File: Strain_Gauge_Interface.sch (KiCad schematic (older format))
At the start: 5 parts, among them U2 INA828

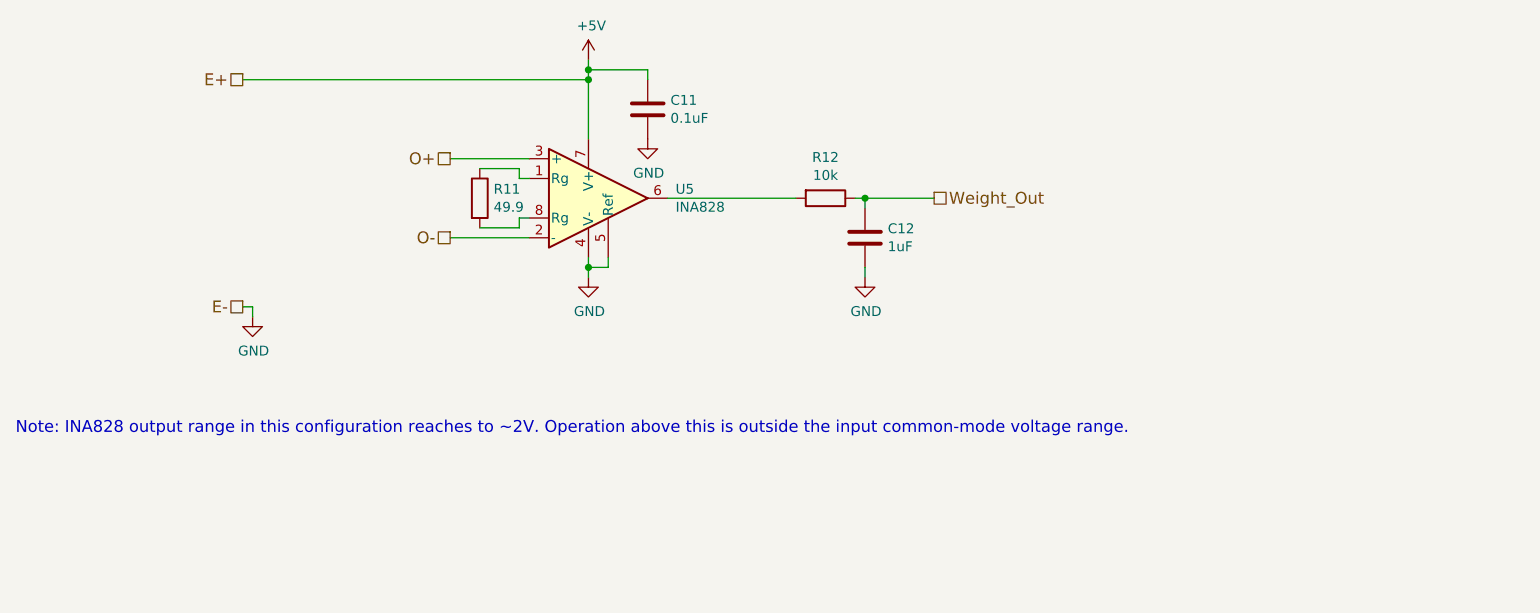
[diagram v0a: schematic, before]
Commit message: Pretty much ready to go. Should verify barrel jack first. Needs a logo.
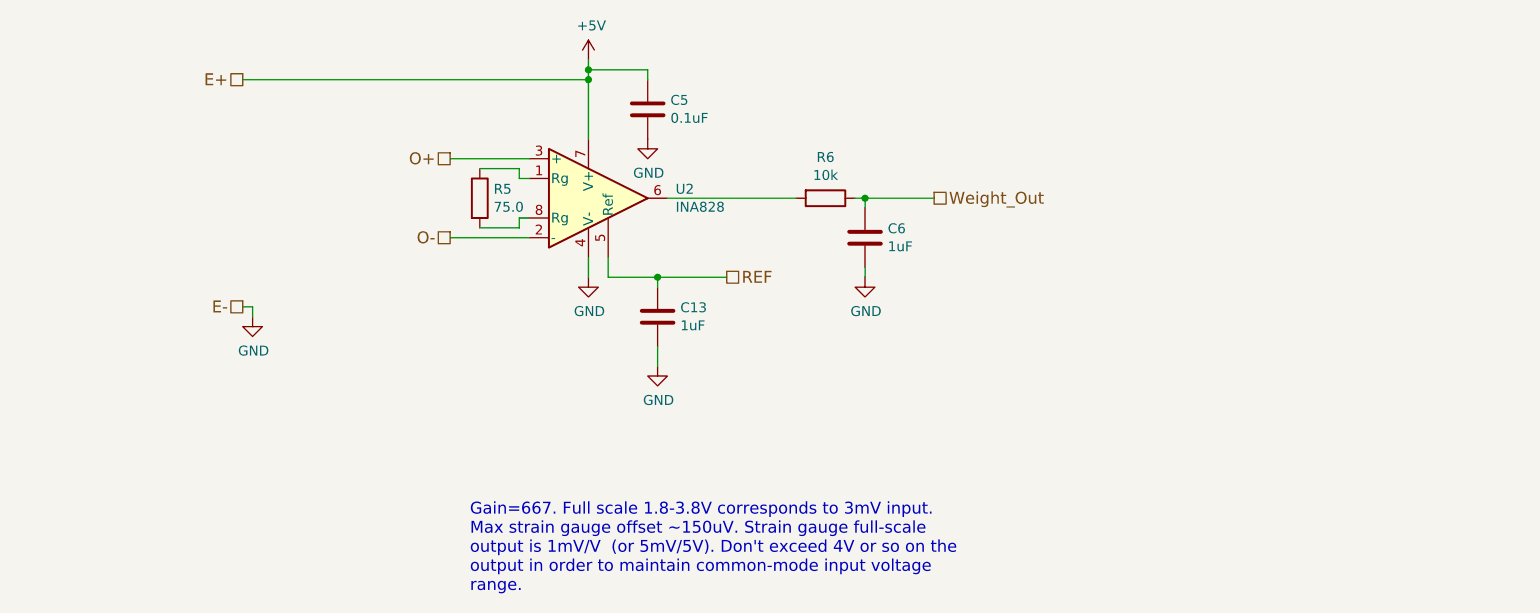
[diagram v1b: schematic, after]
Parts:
- added C16: 1uF, Capacitors_SMD:C_0805_HandSoldering, symbol device:C
- R5: value 49.9 -> 75.0
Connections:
- net GND: now also C16.2; no longer U2.5 (Ref)
- new net REF: C16.1, U2.5 (Ref)
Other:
- note added: "Gain=667. Full scale 1.8-3.8V corresponds to 3mV input.\nMax strain gauge offset ~~150uV. Strain gauge full-scale \noutput is 1mV/V (or 5mV/5V). Don't exceed 4V or so on the\noutput in order to maintain common-mode input voltage\nrange."
- note removed: "Note: INA828 output range in this configuration reaches to ~~2V. Operation above this is outside the input common-mode voltage range."
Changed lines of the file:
@@
 $Descr A4 11693 8268
 encoding utf-8
-Sheet 3 8
+Sheet 7 9
 Title ""
 Date ""
@@
 AR Path="/5A46629B/5A4C63BA" Ref="U3"  Part="1"
 AR Path="/5A4663D1/5A4C63BA" Ref="U4"  Part="1"
-F 0 "U5" H 5041 3546 50  0000 L CNN
+F 0 "U2" H 5041 3546 50  0000 L CNN
 F 1 "INA828" H 5041 3455 50  0000 L CNN
 F 2 "Housings_SOIC:SOIC-8_3.9x4.9mm_Pitch1.27mm" H 4700 3500 50  0001 C CNN
@@
 AR Path="/5A46629B/5A4C64A7" Ref="R7"  Part="1"
 AR Path="/5A4663D1/5A4C64A7" Ref="R9"  Part="1"
-F 0 "R11" H 4120 3546 50  0000 L CNN
-F 1 "49.9" H 4120 3455 50  0000 L CNN
+F 0 "R5" H 4120 3546 50  0000 L CNN
+F 1 "75.0" H 4120 3455 50  0000 L CNN
 F 2 "Resistors_SMD:R_0805_HandSoldering" V 3980 3500 50  0001 C CNN
 F 3 "" H 4050 3500 50  0001 C CNN
@@
 AR Path="/5A46629B/5A4C656F" Ref="C7"  Part="1"
 AR Path="/5A4663D1/5A4C656F" Ref="C9"  Part="1"
-F 0 "C11" H 5015 3096 50  0000 L CNN
+F 0 "C5" H 5015 3096 50  0000 L CNN
 F 1 "0.1uF" H 5015 3005 50  0000 L CNN
 F 2 "Capacitors_SMD:C_0805_HandSoldering" H 4938 2900 50  0001 C CNN
@@
 AR Path="/5A46629B/5A4C6EE8" Ref="R8"  Part="1"
 AR Path="/5A4663D1/5A4C6EE8" Ref="R10"  Part="1"
-F 0 "R12" V 5593 3500 50  0000 C CNN
+F 0 "R6" V 5593 3500 50  0000 C CNN
 F 1 "10k" V 5684 3500 50  0000 C CNN
 F 2 "Resistors_SMD:R_0805_HandSoldering" V 5730 3500 50  0001 C CNN
@@
 AR Path="/5A46629B/5A4C6F98" Ref="C8"  Part="1"
 AR Path="/5A4663D1/5A4C6F98" Ref="C10"  Part="1"
-F 0 "C12" H 6115 3746 50  0000 L CNN
+F 0 "C6" H 6115 3746 50  0000 L CNN
 F 1 "1uF" H 6115 3655 50  0000 L CNN
 F 2 "Capacitors_SMD:C_0805_HandSoldering" H 6038 3550 50  0001 C CNN
@@
 Connection ~ 6000 3500
 Wire Wire Line
-	4600 3800 4600 3850
-Wire Wire Line
 	4600 2850 4600 2900
 Wire Wire Line
@@
 Wire Wire Line
 	4600 2900 4600 3200
-Wire Wire Line
-	4700 3800 4700 3850
-Wire Wire Line
-	4700 3850 4600 3850
-Wire Wire Line
-	4600 3900 4600 3850
-Connection ~ 4600 3850
-Text Notes 1700 4700 0    60   ~ 0
-Note: INA828 output range in this configuration reaches to ~~2V. Operation above this is outside the input common-mode voltage range.
+Text Notes 4000 5500 0    60   ~ 0
+Gain=667. Full scale 1.8-3.8V corresponds to 3mV input.\nMax strain gauge offset ~~150uV. Strain gauge full-scale \noutput is 1mV/V  (or 5mV/5V). Don't exceed 4V or so on the\noutput in order to maintain common-mode input voltage\nrange.
+Text HLabel 5300 3900 2    60   UnSpc ~ 0
+REF
+$Comp
+L device:C C16
+U 1 1 5A4949C9
+P 4950 4100
+AR Path="/5A4665AC/5A4949C9" Ref="C16"  Part="1"
+AR Path="/5A456F58/5A4949C9" Ref="C13"  Part="1"
+AR Path="/5A46629B/5A4949C9" Ref="C14"  Part="1"
+AR Path="/5A4663D1/5A4949C9" Ref="C15"  Part="1"
+F 0 "C13" H 5065 4146 50  0000 L CNN
+F 1 "1uF" H 5065 4055 50  0000 L CNN
+F 2 "Capacitors_SMD:C_0805_HandSoldering" H 4988 3950 50  0001 C CNN
+F 3 "" H 4950 4100 50  0001 C CNN
+	1    4950 4100
+	1    0    0    -1
+$EndComp
+Wire Wire Line
+	4600 3800 4600 3900
+$Comp
+L power:GND #PWR038
+U 1 1 5A494C2C
+P 4950 4350
+AR Path="/5A456F58/5A494C2C" Ref="#PWR038"  Part="1"
+AR Path="/5A46629B/5A494C2C" Ref="#PWR039"  Part="1"
+AR Path="/5A4663D1/5A494C2C" Ref="#PWR040"  Part="1"
+AR Path="/5A4665AC/5A494C2C" Ref="#PWR041"  Part="1"
+F 0 "#PWR041" H 4950 4100 50  0001 C CNN
+F 1 "GND" H 4955 4177 50  0000 C CNN
+F 2 "" H 4950 4350 50  0001 C CNN
+F 3 "" H 4950 4350 50  0001 C CNN
+	1    4950 4350
+	1    0    0    -1
+$EndComp
+Wire Wire Line
+	4700 3800 4700 3900
+Wire Wire Line
+	4700 3900 4950 3900
+Wire Wire Line
+	4950 3950 4950 3900
+Connection ~ 4950 3900
+Wire Wire Line
+	4950 3900 5300 3900
+Wire Wire Line
+	4950 4250 4950 4350
 $EndSCHEMATC
